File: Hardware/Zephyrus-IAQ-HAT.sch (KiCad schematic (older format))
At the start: 6 parts, among them J1 Conn_02x20_Odd_Even__Rpi, J2 USART

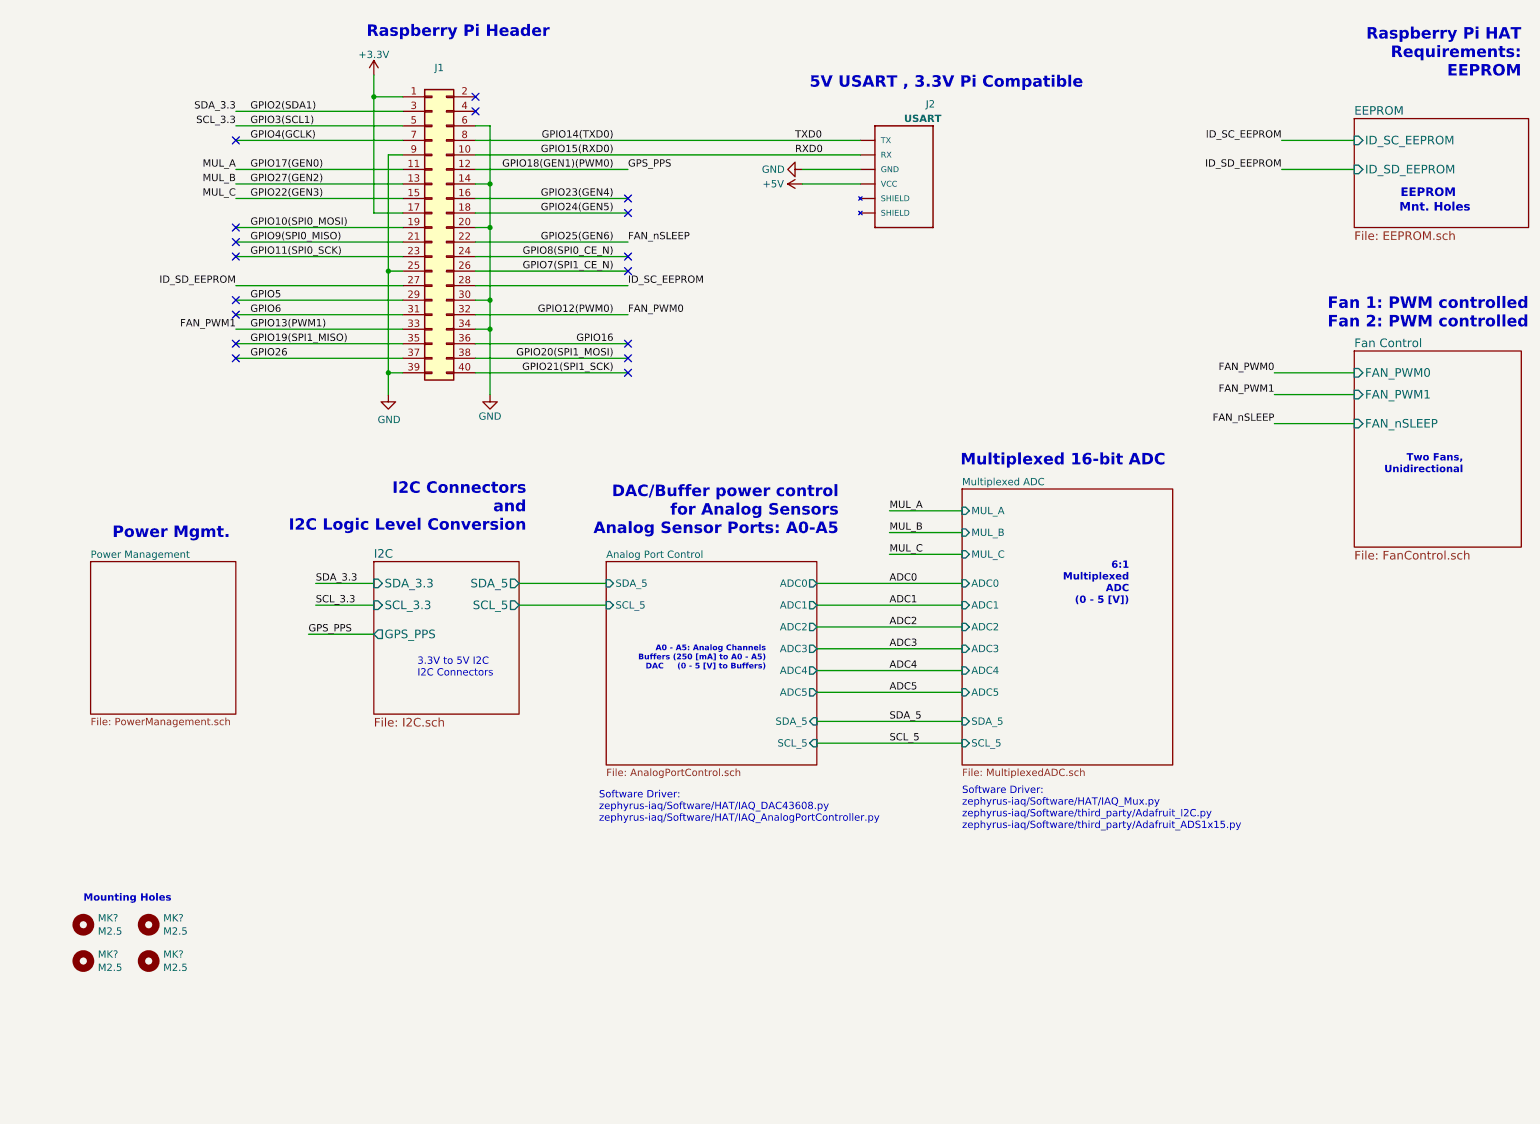
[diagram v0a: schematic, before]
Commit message: Up Changed I2C addres for DAC and ADC.  Added MOSFET to USART RX.
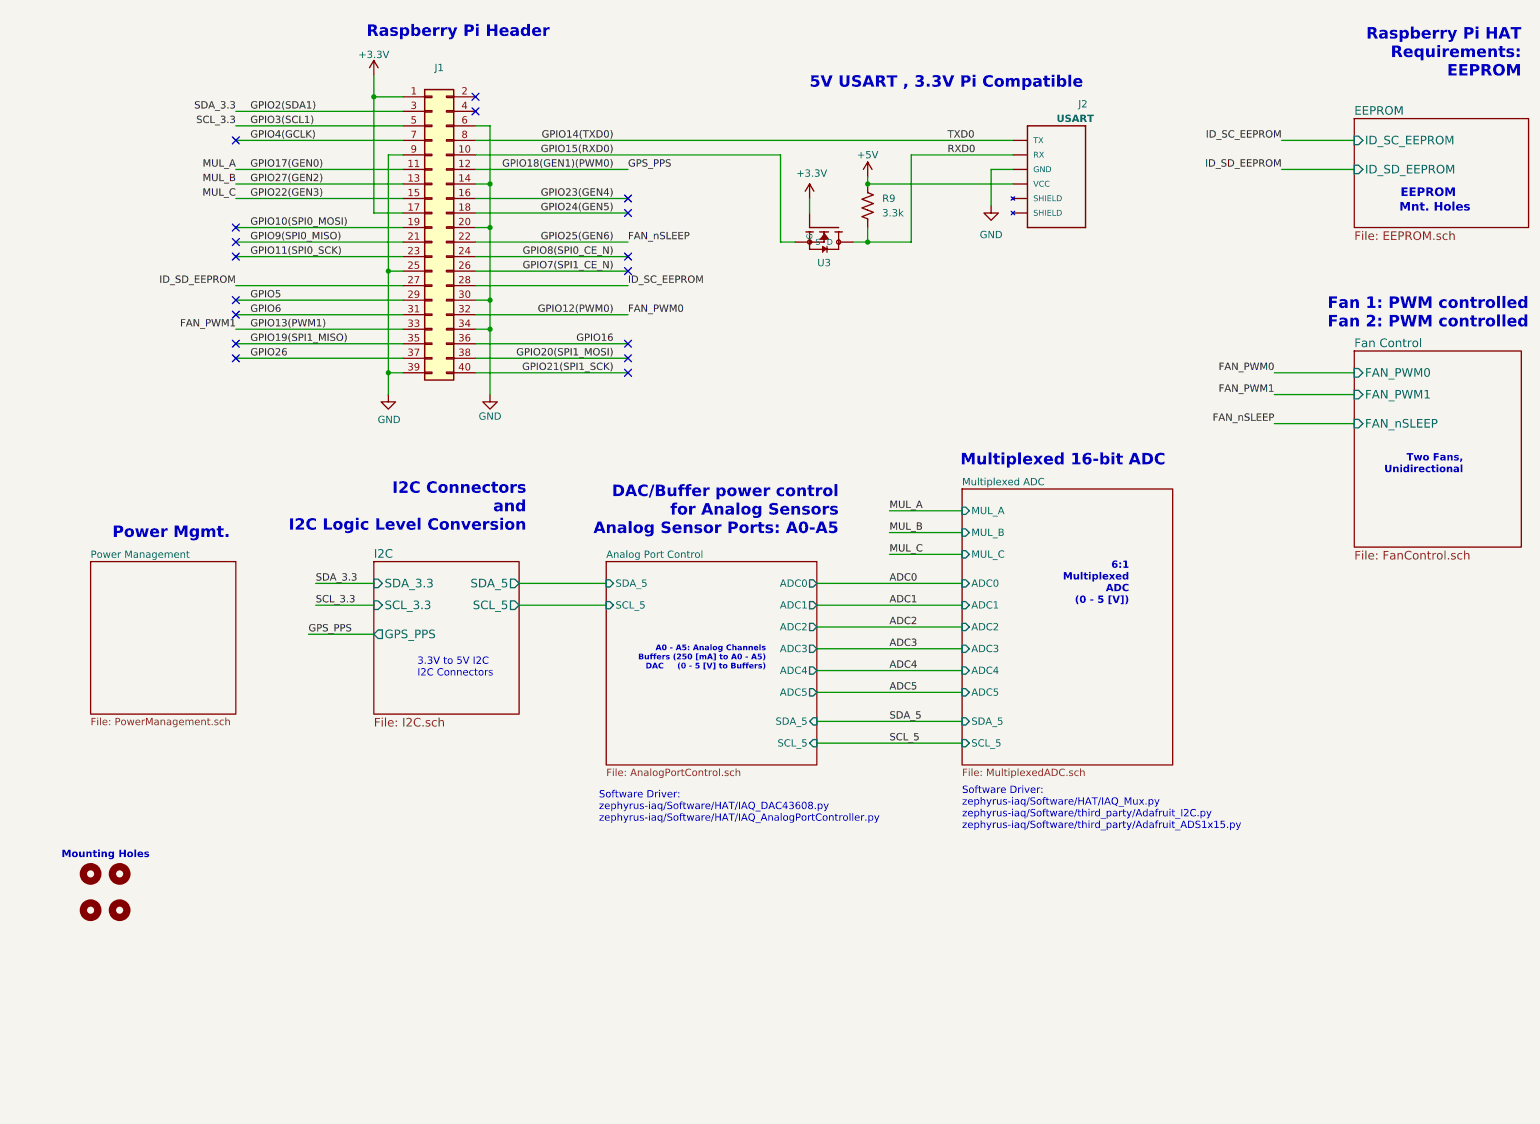
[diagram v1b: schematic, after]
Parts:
- added R9: 3.3k, Resistor_SMD:R_0805_2012Metric, symbol zephyrus_iaq:R_US
- added U3: BSS138, zephyrus-iaq:BSS138, symbol zephyrus_iaq:BSS138
- gave numbers to parts that had none: 4
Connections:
- net +3V3: now also U3.G
- net +5V: now also R9.1
- net GPIO15(RXD0): now also U3.S; no longer J2.2 (RX)
- new net RXD0: J2.2 (RX), R9.2, U3.D
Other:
- moved on the sheet: J2
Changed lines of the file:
@@
 EESchema Schematic File Version 4
-LIBS:TopLevel-cache
 EELAYER 30 0
 EELAYER END
@@
 Title "Top Level"
 Date "2019-11-15"
-Rev ""
+Rev "A"
 Comp "Zephyrus, Indoor Air Quality - Raspberry Pi HAT"
 Comment1 ""
@@
 	1    0    0    -1
 $EndComp
-$Comp
-L zephyrus_iaq:SM04B-SRSS-TB(LF)(SN)_USART J2
-U 1 1 5D996B28
-P 6600 1700
-F 0 "J2" H 6750 2150 50  0000 L CNN
-F 1 "USART" H 6600 2050 50  0000 L CNB
-F 2 "zephyrus-iaq:JST_SM04B-SRSS-TB(LF)(SN)" H 6650 1800 50  0001 C CNN
-F 3 "" H 6650 1800 50  0001 C CNN
-	1    6600 1700
-	1    0    0    -1
-$EndComp
-Text Notes 5950 1150 0    79   ~ 16
-5V USART , 3.3V Pi Compatible
 Text Label 6500 4550 0    50   ~ 0
 ADC0
@@
 Text Label 2000 2500 2    50   ~ 0
 ID_SD_EEPROM
-$Comp
-L zephyrus_iaq:+5V #PWR09
-U 1 1 5D96FDD5
-P 5900 1800
-F 0 "#PWR09" H 5900 1650 50  0001 C CNN
-F 1 "+5V" V 5900 2000 50  0000 C CNN
-F 2 "" H 5900 1800 50  0001 C CNN
-F 3 "" H 5900 1800 50  0001 C CNN
-	1    5900 1800
-	0    -1   -1   0
-$EndComp
-$Comp
-L zephyrus_iaq:GND #PWR08
-U 1 1 5D9839C0
-P 5900 1700
-F 0 "#PWR08" H 5900 1450 50  0001 C CNN
-F 1 "GND" V 5900 1500 50  0000 C CNN
-F 2 "" H 5900 1700 50  0001 C CNN
-F 3 "" H 5900 1700 50  0001 C CNN
-	1    5900 1700
-	0    1    1    0
-$EndComp
-Text Label 5850 1600 0    50   ~ 0
-RXD0
-Text Label 5850 1500 0    50   ~ 0
-TXD0
 Wire Wire Line
 	3150 1600 3050 1600
@@
 Text Label 4700 1700 0    50   ~ 0
 GPS_PPS
-Wire Wire Line
-	5900 1700 6300 1700
-Wire Wire Line
-	5900 1800 6300 1800
 $Sheet
 S 1000 4400 1000 1050
@@
 Wire Wire Line
 	2950 4900 2500 4900
-Wire Wire Line
-	3650 1600 6300 1600
-Wire Wire Line
-	3650 1500 6300 1500
 Text Notes 10450 3800 2    50   ~ 10
 Two Fans, \nUnidirectional
@@
 Raspberry Pi Header
 $Comp
-L zephyrus_iaq:Mounting-Hole-Mechanical MK?
+L zephyrus_iaq:Mounting-Hole-Mechanical MK4
 U 1 1 5DD01D93
-P 1400 7050
-AR Path="/5DD01D93" Ref="MK?"  Part="1"
+P 1200 6700
+AR Path="/5DD01D93" Ref="MK4"  Part="1"
 AR Path="/5DAFB35B/5DD01D93" Ref="MK?"  Part="1"
-F 0 "MK?" H 1500 6996 50  0000 L CNN
-F 1 "M2.5" H 1500 6905 50  0000 L CNN
-F 2 "MountingHole:MountingHole_2.7mm_M2.5" H 1400 7050 50  0001 C CNN
-F 3 "" H 1400 7050 50  0001 C CNN
-	1    1400 7050
-	1    0    0    -1
-$EndComp
-$Comp
-L zephyrus_iaq:Mounting-Hole-Mechanical MK?
+F 0 "MK4" H 1300 6646 50  0001 L CNN
+F 1 "M2.5" H 1300 6555 50  0001 L CNN
+F 2 "MountingHole:MountingHole_2.7mm_M2.5" H 1200 6700 50  0001 C CNN
+F 3 "" H 1200 6700 50  0001 C CNN
+	1    1200 6700
+	1    0    0    -1
+$EndComp
+$Comp
+L zephyrus_iaq:Mounting-Hole-Mechanical MK2
 U 1 1 5DD01D99
-P 1400 6800
-AR Path="/5DD01D99" Ref="MK?"  Part="1"
+P 1200 6450
+AR Path="/5DD01D99" Ref="MK2"  Part="1"
 AR Path="/5DAFB35B/5DD01D99" Ref="MK?"  Part="1"
-F 0 "MK?" H 1500 6746 50  0000 L CNN
-F 1 "M2.5" H 1500 6655 50  0000 L CNN
-F 2 "MountingHole:MountingHole_2.7mm_M2.5" H 1400 6800 50  0001 C CNN
-F 3 "" H 1400 6800 50  0001 C CNN
-	1    1400 6800
-	1    0    0    -1
-$EndComp
-$Comp
-L zephyrus_iaq:Mounting-Hole-Mechanical MK?
+F 0 "MK2" H 1300 6396 50  0001 L CNN
+F 1 "M2.5" H 1300 6305 50  0001 L CNN
+F 2 "MountingHole:MountingHole_2.7mm_M2.5" H 1200 6450 50  0001 C CNN
+F 3 "" H 1200 6450 50  0001 C CNN
+	1    1200 6450
+	1    0    0    -1
+$EndComp
+$Comp
+L zephyrus_iaq:Mounting-Hole-Mechanical MK3
 U 1 1 5DD01D9F
-P 950 7050
-AR Path="/5DD01D9F" Ref="MK?"  Part="1"
+P 1000 6700
+AR Path="/5DD01D9F" Ref="MK3"  Part="1"
 AR Path="/5DAFB35B/5DD01D9F" Ref="MK?"  Part="1"
-F 0 "MK?" H 1050 6996 50  0000 L CNN
-F 1 "M2.5" H 1050 6905 50  0000 L CNN
-F 2 "MountingHole:MountingHole_2.7mm_M2.5" H 950 7050 50  0001 C CNN
-F 3 "" H 950 7050 50  0001 C CNN
-	1    950  7050
-	1    0    0    -1
-$EndComp
-$Comp
-L zephyrus_iaq:Mounting-Hole-Mechanical MK?
+F 0 "MK3" H 1100 6646 50  0001 L CNN
+F 1 "M2.5" H 1100 6555 50  0001 L CNN
+F 2 "MountingHole:MountingHole_2.7mm_M2.5" H 1000 6700 50  0001 C CNN
+F 3 "" H 1000 6700 50  0001 C CNN
+	1    1000 6700
+	1    0    0    -1
+$EndComp
+$Comp
+L zephyrus_iaq:Mounting-Hole-Mechanical MK1
 U 1 1 5DD01DA5
-P 950 6800
-AR Path="/5DD01DA5" Ref="MK?"  Part="1"
+P 1000 6450
+AR Path="/5DD01DA5" Ref="MK1"  Part="1"
 AR Path="/5DAFB35B/5DD01DA5" Ref="MK?"  Part="1"
-F 0 "MK?" H 1050 6746 50  0000 L CNN
-F 1 "M2.5" H 1050 6655 50  0000 L CNN
-F 2 "MountingHole:MountingHole_2.7mm_M2.5" H 950 6800 50  0001 C CNN
-F 3 "" H 950 6800 50  0001 C CNN
-	1    950  6800
-	1    0    0    -1
-$EndComp
-Text Notes 950  6750 0    50   ~ 10
+F 0 "MK1" H 1100 6396 50  0001 L CNN
+F 1 "M2.5" H 1100 6305 50  0001 L CNN
+F 2 "MountingHole:MountingHole_2.7mm_M2.5" H 1000 6450 50  0001 C CNN
+F 3 "" H 1000 6450 50  0001 C CNN
+	1    1000 6450
+	1    0    0    -1
+$EndComp
+Text Notes 800  6450 0    50   ~ 10
 Mounting Holes
+Wire Wire Line
+	5950 1900 5950 2000
+$Comp
+L zephyrus_iaq:BSS138 U?
+U 1 1 5DE9F97B
+P 6050 2100
+AR Path="/5DB861AF/5DE9F97B" Ref="U?"  Part="1"
+AR Path="/5DE9F97B" Ref="U3"  Part="1"
+F 0 "U3" V 6293 2100 50  0000 C CNN
+F 1 "BSS138" V 6384 2100 50  0001 C CNN
+F 2 "zephyrus-iaq:BSS138" H 6500 2800 50  0001 L BNN
+F 3 "TO-236-3 Micross" H 6500 2600 50  0001 L BNN
+F 4 "MICROSS/On Semiconductor" H 6500 2500 50  0001 L BNN "Field4"
+F 5 "Mosfet n-Ch 50v 220ma Die" H 6500 2350 50  0001 L BNN "Field5"
+F 6 "BSS138" H 6500 2700 50  0001 L BNN "Field7"
+	1    6050 2100
+	0    1    1    0
+$EndComp
+$Comp
+L zephyrus_iaq:R_US R?
+U 1 1 5DE9F972
+P 6350 1950
+AR Path="/5DB861AF/5DE9F972" Ref="R?"  Part="1"
+AR Path="/5DE9F972" Ref="R9"  Part="1"
+F 0 "R9" H 6450 2000 50  0000 L CNN
+F 1 "3.3k" H 6450 1900 50  0000 L CNN
+F 2 "Resistor_SMD:R_0805_2012Metric" V 6390 1940 50  0001 C CNN
+F 3 "~" H 6350 1950 50  0001 C CNN
+	1    6350 1950
+	1    0    0    -1
+$EndComp
+Wire Wire Line
+	5750 2200 5850 2200
+Wire Wire Line
+	6250 2200 6350 2200
+Wire Wire Line
+	6350 2200 6350 2100
+$Comp
+L zephyrus_iaq:+3.3V #PWR?
+U 1 1 5DE9F969
+P 5950 1900
+AR Path="/5DB861AF/5DE9F969" Ref="#PWR?"  Part="1"
+AR Path="/5DE9F969" Ref="#PWR0109"  Part="1"
+F 0 "#PWR0109" H 5950 1750 50  0001 C CNN
+F 1 "+3.3V" H 5965 2073 50  0000 C CNN
+F 2 "" H 5950 1900 50  0001 C CNN
+F 3 "" H 5950 1900 50  0001 C CNN
+	1    5950 1900
+	1    0    0    -1
+$EndComp
+Text Label 6900 1500 0    50   ~ 0
+TXD0
+Text Label 6900 1600 0    50   ~ 0
+RXD0
+$Comp
+L zephyrus_iaq:GND #PWR08
+U 1 1 5D9839C0
+P 7200 1950
+F 0 "#PWR08" H 7200 1700 50  0001 C CNN
+F 1 "GND" H 7200 1750 50  0000 C CNN
+F 2 "" H 7200 1950 50  0001 C CNN
+F 3 "" H 7200 1950 50  0001 C CNN
+	1    7200 1950
+	1    0    0    -1
+$EndComp
+Text Notes 5950 1150 0    79   ~ 16
+5V USART , 3.3V Pi Compatible
+$Comp
+L zephyrus_iaq:SM04B-SRSS-TB(LF)(SN)_USART J2
+U 1 1 5D996B28
+P 7650 1700
+F 0 "J2" H 7800 2150 50  0000 L CNN
+F 1 "USART" H 7650 2050 50  0000 L CNB
+F 2 "zephyrus-iaq:JST_SM04B-SRSS-TB(LF)(SN)" H 7700 1800 50  0001 C CNN
+F 3 "" H 7700 1800 50  0001 C CNN
+	1    7650 1700
+	1    0    0    -1
+$EndComp
+Wire Wire Line
+	6350 2200 6650 2200
+Wire Wire Line
+	6650 2200 6650 1600
+Connection ~ 6350 2200
+Wire Wire Line
+	6650 1600 7350 1600
+Wire Wire Line
+	7350 1700 7200 1700
+Wire Wire Line
+	7200 1700 7200 1950
+Wire Wire Line
+	6350 1800 7350 1800
+$Comp
+L zephyrus_iaq:+5V #PWR?
+U 1 1 5DE9F963
+P 6350 1750
+AR Path="/5DB861AF/5DE9F963" Ref="#PWR?"  Part="1"
+AR Path="/5DE9F963" Ref="#PWR0110"  Part="1"
+F 0 "#PWR0110" H 6350 1600 50  0001 C CNN
+F 1 "+5V" H 6350 1900 50  0000 C CNN
+F 2 "" H 6350 1750 50  0001 C CNN
+F 3 "" H 6350 1750 50  0001 C CNN
+	1    6350 1750
+	1    0    0    -1
+$EndComp
+Wire Wire Line
+	6350 1750 6350 1800
+Connection ~ 6350 1800
+Wire Wire Line
+	5750 1600 5750 2200
+Wire Wire Line
+	3650 1600 5750 1600
+Wire Wire Line
+	3650 1500 7350 1500
 $EndSCHEMATC

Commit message: Updated Schematic Attribution and Documentation
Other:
- note added: "Raspberry Pi 3.3V TX can register HIGH on 5V TTL compatible USART"
- note added: "SCL/SDA 5V is on the same I2C bus as 3.3V SCL/SDA"
- note added: "Step the TX line from target device \ndown for 3.3V RX on Raspbery line\nSimiliar BSS138 circuit as I2C logic level shifting."
- moved on the sheet: J1, J2, R9, U3
